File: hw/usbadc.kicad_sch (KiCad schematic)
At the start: 14 parts, among them U6 PCA9306DC1, U8 24AA0x, X1 ECS-2520MV-260-CN-TR

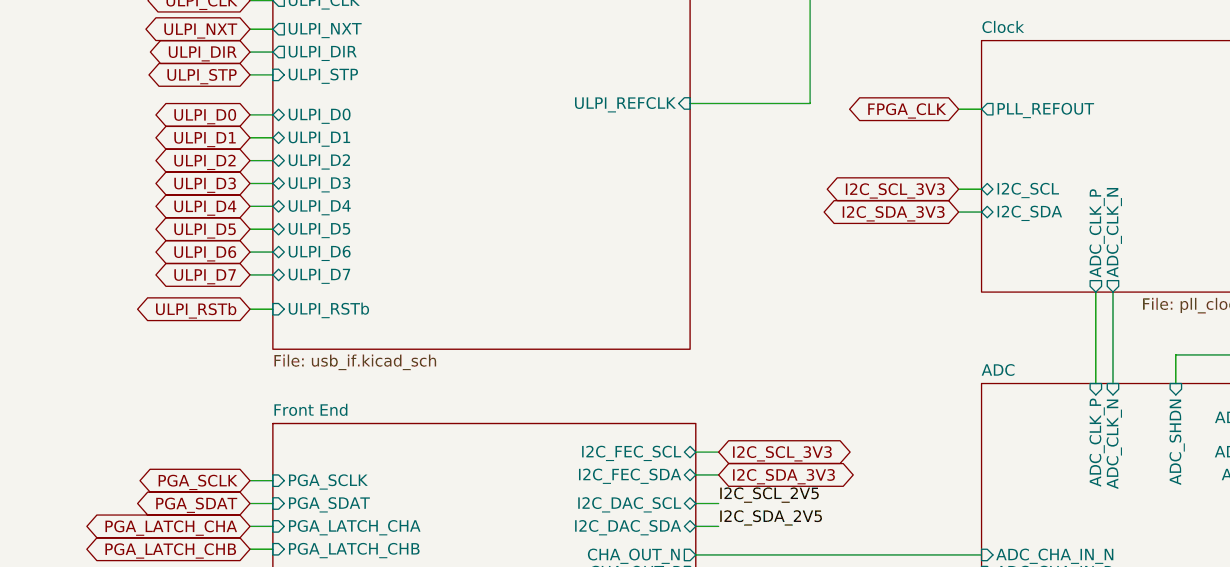
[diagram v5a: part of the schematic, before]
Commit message: connected versaclock CLKSEL to ULPI RSTB (share FPGA pin)
ULPI Rstb is unlikely to be used

Also: - update of kicad to 9.0 (many library footprints updated)
      - added sheet titles, author
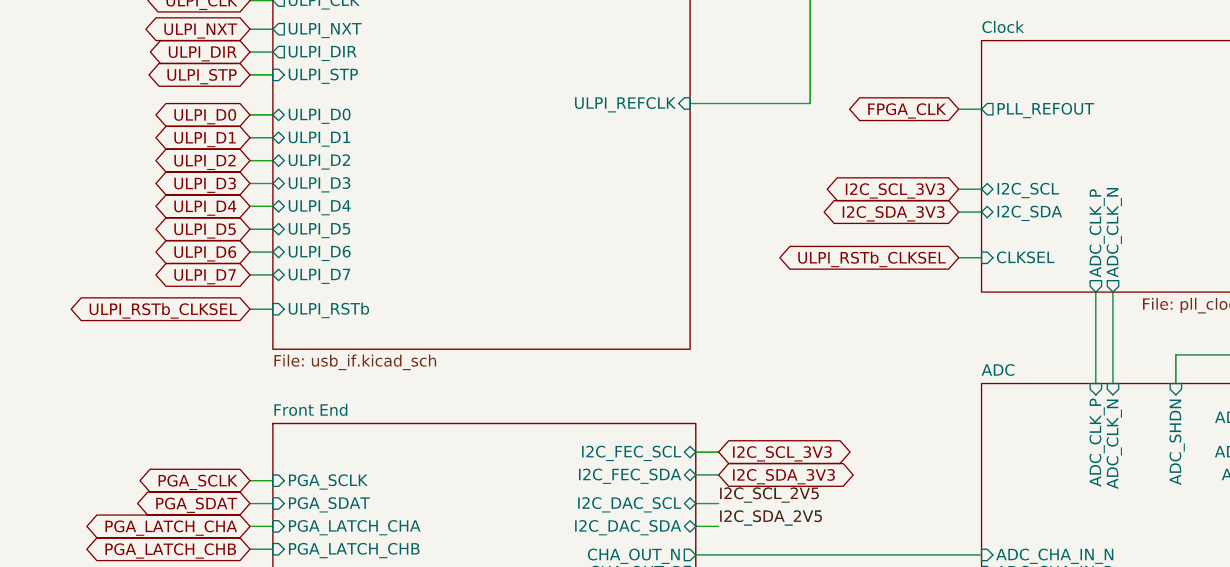
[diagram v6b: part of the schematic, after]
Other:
- sheet Clock ports: added CLKSEL; removed none
- company: (none) -> Till Straumann
- title: (none) -> 130MSPS Dual-Channel USB Scope
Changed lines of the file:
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@@
 (kicad_sch
-	(version 20231120)
+	(version 20250114)
 	(generator "eeschema")
-	(generator_version "8.0")
+	(generator_version "9.0")
 	(paper "A4")
+	(title_block
+		(title "130MSPS Dual-Channel USB Scope")
+		(rev "3.3b")
+		(company "Till Straumann")
+	)
+	(text "Optional EEPROM. Nonvolatile\ndata may as well be stored in\nunused flash area."
+		(exclude_from_sim no)
+		(at 248.92 130.81 0)
+		(effects
+			(font
+				(size 1.27 1.27)
+			)
+			(justify left bottom)
+		)
+	)
+	(text "When generating the ULPI refclk\nwith the VersaClock then remove\nX1 and load R117."
+		(exclude_from_sim no)
+		(at 184.15 73.025 0)
+		(effects
+			(font
+				(size 1.27 1.27)
+			)
+			(justify left bottom)
+		)
+	)
+	(text "Populate either R123 or R124\ndepending on desired I/O voltage\nlevel.\nEven for 3V3, the *input* should\nbe 5V tolerant."
+		(exclude_from_sim no)
+		(at 76.2 54.61 0)
+		(effects
+			(font
+				(size 1.27 1.27)
+			)
+			(justify left bottom)
+		)
+	)
 	(junction
 		(at 85.725 40.64)
@@
 	(wire
 		(pts
+			(xy 128.905 97.155) (xy 131.445 97.155)
+		)
+		(stroke
+			(width 0)
+			(type default)
+		)
+	)
+	(wire
+		(pts
 			(xy 168.275 147.955) (xy 170.815 147.955)
 		)
@@
 		)
 	)
-	(text "Optional EEPROM. Nonvolatile\ndata may as well be stored in\nunused flash area."
-		(exclude_from_sim no)
-		(at 248.92 130.81 0)
-		(effects
-			(font
-				(size 1.27 1.27)
-			)
-			(justify left bottom)
-		)
-	)
-	(text "When generating the ULPI refclk\nwith the VersaClock then remove\nX1 and load R117."
-		(exclude_from_sim no)
-		(at 184.15 73.025 0)
-		(effects
-			(font
-				(size 1.27 1.27)
-			)
-			(justify left bottom)
-		)
-	)
-	(text "Populate either R123 or R124\ndepending on desired I/O voltage\nlevel.\nEven for 3V3, the *input* should\nbe 5V tolerant."
-		(exclude_from_sim no)
-		(at 76.2 54.61 0)
-		(effects
-			(font
-				(size 1.27 1.27)
-			)
-			(justify left bottom)
-		)
-	)
 	(label "PWR_GOOD"
 		(at 230.505 51.435 0)
@@
 		)
 	)
-	(global_label "ULPI_RSTb"
-		(shape bidirectional)
-		(at 50.165 102.87 180)
-		(fields_autoplaced yes)
-		(effects
-			(font
-				(size 1.27 1.27)
-			)
-			(justify right)
-		)
-		(property "Intersheetrefs" "${INTERSHEET_REFS}"
-			(at 37.0844 102.87 0)
-			(effects
-				(font
-					(size 1.27 1.27)
-				)
-				(justify right)
-				(hide yes)
-			)
-		)
-	)
 	(global_label "GPIO_DIR"
 		(shape bidirectional)
@@
 		)
 	)
+	(global_label "ULPI_RSTb_CLKSEL"
+		(shape bidirectional)
+		(at 50.165 102.87 180)
+		(fields_autoplaced yes)
+		(effects
+			(font
+				(size 1.27 1.27)
+			)
+			(justify right)
+		)
+		(property "Intersheetrefs" "${INTERSHEET_REFS}"
+			(at 29.1621 102.87 0)
+			(effects
+				(font
+					(size 1.27 1.27)
+				)
+				(justify right)
+				(hide yes)
+			)
+		)
+	)
 	(global_label "ADC_D5"
 		(shape bidirectional)
@@
 		)
 	)
+	(global_label "ULPI_RSTb_CLKSEL"
+		(shape bidirectional)
+		(at 128.905 97.155 180)
+		(fields_autoplaced yes)
+		(effects
+			(font
+				(size 1.27 1.27)
+			)
+			(justify right)
+		)
+		(property "Intersheetrefs" "${INTERSHEET_REFS}"
+			(at 107.9021 97.155 0)
+			(effects
+				(font
+					(size 1.27 1.27)
+				)
+				(justify right)
+				(hide yes)
+			)
+		)
+	)
 	(global_label "ADC_D6"
 		(shape bidirectional)
@@
 		(on_board yes)
 		(dnp no)
-		(property "Reference" "#PWR?"
+		(property "Reference" "#PWR0128"
 			(at 78.105 35.56 0)
 			(effects
@@
 		(at 235.585 147.32)
 		(size 40.64 14.605)
+		(exclude_from_sim no)
+		(in_bom yes)
+		(on_board yes)
+		(dnp no)
 		(fields_autoplaced yes)
 		(stroke
@@
 		(at 131.445 73.025)
 		(size 36.83 27.94)
+		(exclude_from_sim no)
+		(in_bom yes)
+		(on_board yes)
+		(dnp no)
 		(stroke
 			(width 0)
@@
 			)
 		)
+		(pin "CLKSEL" input
+			(at 131.445 97.155 180)
+			(effects
+				(font
+					(size 1.27 1.27)
+				)
+				(justify left)
+			)
+		)
 		(instances
 			(project "usbadc"
@@
 		(at 131.445 111.125)
 		(size 36.83 50.165)
+		(exclude_from_sim no)
+		(in_bom yes)
+		(on_board yes)
+		(dnp no)
 		(fields_autoplaced yes)
 		(stroke
@@
 		(at 259.08 50.165)
 		(size 16.51 60.96)
+		(exclude_from_sim no)
+		(in_bom yes)
+		(on_board yes)
+		(dnp no)
 		(fields_autoplaced yes)
 		(stroke
@@
 		(at 52.705 38.1)
 		(size 21.59 15.24)
+		(exclude_from_sim no)
+		(in_bom yes)
+		(on_board yes)
+		(dnp no)
 		(fields_autoplaced yes)
 		(stroke
@@
 		(at 52.705 66.675)
 		(size 46.355 40.64)
+		(exclude_from_sim no)
+		(in_bom yes)
+		(on_board yes)
+		(dnp no)
 		(fields_autoplaced yes)
 		(stroke
@@
 		(at 52.705 115.57)
 		(size 46.99 26.67)
+		(exclude_from_sim no)
+		(in_bom yes)
+		(on_board yes)
+		(dnp no)
 		(fields_autoplaced yes)
 		(stroke
@@
 		(at 204.47 31.115)
 		(size 22.86 27.94)
+		(exclude_from_sim no)
+		(in_bom yes)
+		(on_board yes)
+		(dnp no)
 		(fields_autoplaced yes)
 		(stroke
@@
 		)
 	)
+	(embedded_fonts no)
 )

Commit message: Added licensing information
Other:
- company: Till Straumann -> Copyright Till Straumann, 2025
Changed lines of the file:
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@@
 		(title "130MSPS Dual-Channel USB Scope")
 		(rev "3.3b")
-		(company "Till Straumann")
+		(company "Copyright Till Straumann, 2025")
+		(comment 1 "License: CERN-OHL-P v2")
 	)
 	(text "Optional EEPROM. Nonvolatile\ndata may as well be stored in\nunused flash area."
